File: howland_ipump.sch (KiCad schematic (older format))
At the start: 10 parts, among them U11 OPA991S

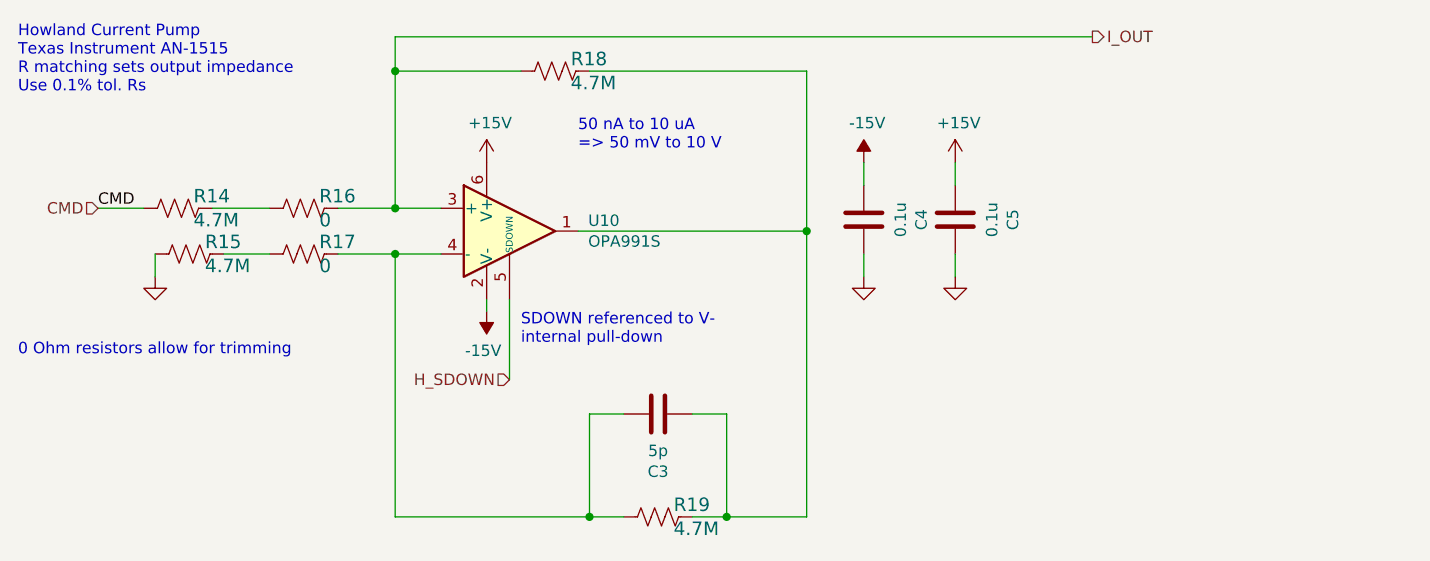
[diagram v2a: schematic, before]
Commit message: near complete top level schematic routing
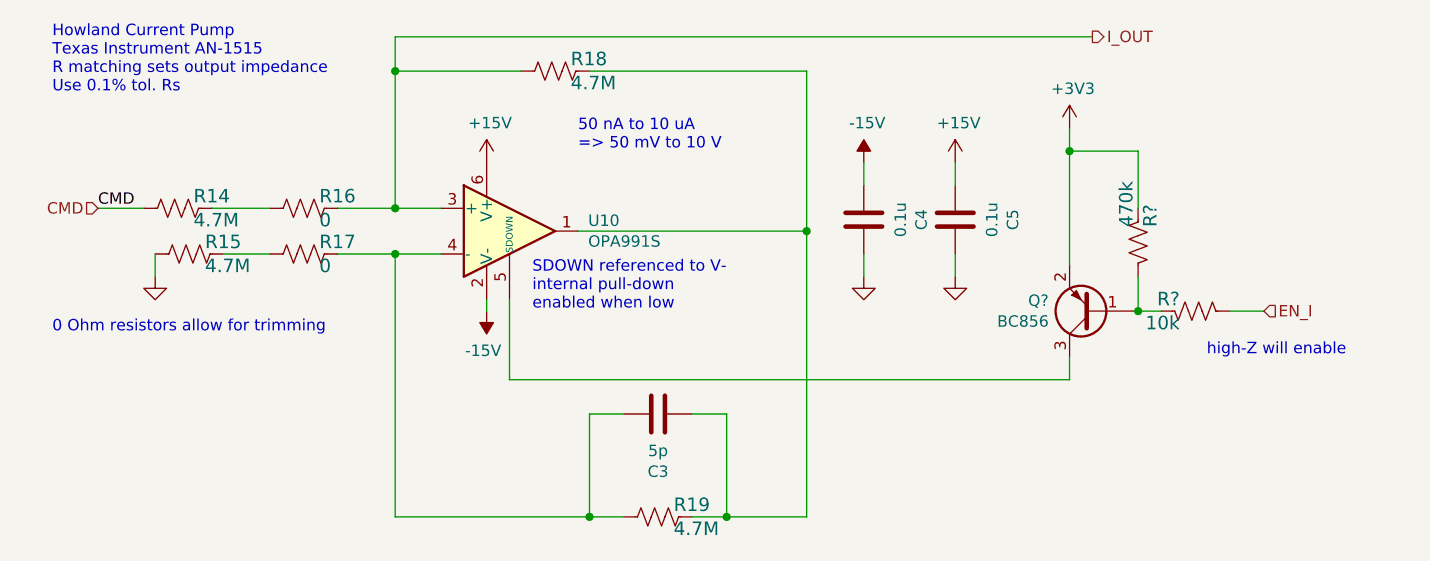
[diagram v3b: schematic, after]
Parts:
- added Q?: BC856, Package_TO_SOT_SMD:SOT-23, symbol Transistor_BJT:BC856
- added R?: 10k, Resistor_SMD:R_0603_1608Metric, symbol Device:R_US
- added R?: 470k, Resistor_SMD:R_0603_1608Metric, symbol Device:R_US
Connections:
- net H_SDOWN: no longer names the net of U11.5 (SDOWN)
- net H_SDOWN: now also Q?.3 (C)
- new net: Q?.1 (B), R?.1, R?.2
- new net +3V3: Q?.2 (E), R?.1
- new net EN_I: R?.2
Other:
- note added: "SDOWN referenced to V-\ninternal pull-down\nenabled when low\n"
- note added: "high-Z will enable"
- note removed: "SDOWN referenced to V-\ninternal pull-down\n"
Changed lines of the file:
@@
 $Descr A4 11693 8268
 encoding utf-8
-Sheet 4 18
+Sheet 3 18
 Title ""
 Date ""
@@
 AR Path="/6095BD4C/60BE01FC/60D781E3" Ref="#PWR0116"  Part="1"
 AR Path="/6095BD4C/60C5A41E/60D781E3" Ref="#PWR?"  Part="1"
+AR Path="/61B02572/60BE01FC/60D781E3" Ref="#PWR?"  Part="1"
 F 0 "#PWR0116" H 5100 4150 50  0001 C CNN
 F 1 "-15V" H 5115 4223 50  0000 C CNN
@@
 AR Path="/6095BD4C/60BE01FC/60D781E9" Ref="#PWR0157"  Part="1"
 AR Path="/6095BD4C/60C5A41E/60D781E9" Ref="#PWR?"  Part="1"
+AR Path="/61B02572/60BE01FC/60D781E9" Ref="#PWR?"  Part="1"
 F 0 "#PWR0157" H 5100 3250 50  0001 C CNN
 F 1 "+15V" H 5115 3573 50  0000 C CNN
@@
 AR Path="/6095BD4C/60BE01FC/60D781F4" Ref="C3"  Part="1"
 AR Path="/6095BD4C/60C5A41E/60D781F4" Ref="C?"  Part="1"
+AR Path="/61B02572/60BE01FC/60D781F4" Ref="C?"  Part="1"
 F 0 "C3" V 5598 4500 50  0000 C CNN
 F 1 "5p" V 5689 4500 50  0000 C CNN
@@
 AR Path="/6095BD4C/60BE01FC/60D78215" Ref="#PWR0158"  Part="1"
 AR Path="/6095BD4C/60C5A41E/60D78215" Ref="#PWR?"  Part="1"
+AR Path="/61B02572/60BE01FC/60D78215" Ref="#PWR?"  Part="1"
 F 0 "#PWR0158" H 3650 3650 50  0001 C CNN
 F 1 "GND" V 3655 3772 50  0001 R CNN
@@
 AR Path="/6095BD4C/60BE01FC/60D7821F" Ref="U10"  Part="1"
 AR Path="/6095BD4C/60C5A41E/60D7821F" Ref="U?"  Part="1"
+AR Path="/61B02572/60BE01FC/60D7821F" Ref="U?"  Part="1"
 F 0 "U10" H 5544 3746 50  0000 L CNN
 F 1 "OPA991S" H 5544 3655 50  0000 L CNN
@@
 Wire Wire Line
 	5550 3000 6500 3000
-Text Notes 5250 4200 0    50   ~ 0
-SDOWN referenced to V-\ninternal pull-down\n
-Wire Wire Line
-	5200 4000 5200 4350
+Text Notes 5300 4050 0    50   ~ 0
+SDOWN referenced to V-\ninternal pull-down\nenabled when low\n
 Text Notes 5500 3350 0    50   ~ 0
 50 nA to 10 uA\n=> 50 mV to 10 V
@@
 AR Path="/6095BD4C/60BE01FC/60D78240" Ref="R19"  Part="1"
 AR Path="/6095BD4C/60C5A41E/60D78240" Ref="R?"  Part="1"
+AR Path="/61B02572/60BE01FC/60D78240" Ref="R?"  Part="1"
 F 0 "R19" V 5797 5018 59  0000 L CNN
 F 1 "4.7M" V 5902 5018 59  0000 L CNN
@@
 	0    1    1    0
 $EndComp
-Text Notes 3050 3100 0    50   ~ 0
+Text Notes 3200 3100 0    50   ~ 0
 Howland Current Pump\nTexas Instrument AN-1515\nR matching sets output impedance\nUse 0.1% tol. Rs
 $Comp
@@
 AR Path="/6095BD4C/60BE01FC/60D7824A" Ref="C4"  Part="1"
 AR Path="/6095BD4C/60C5A41E/60D7824A" Ref="C?"  Part="1"
+AR Path="/61B02572/60BE01FC/60D7824A" Ref="C?"  Part="1"
 F 0 "C4" V 6498 3650 50  0000 C CNN
 F 1 "0.1u" V 6589 3650 50  0000 C CNN
@@
 AR Path="/6095BD4C/60BE01FC/60D78250" Ref="#PWR0163"  Part="1"
 AR Path="/6095BD4C/60C5A41E/60D78250" Ref="#PWR?"  Part="1"
+AR Path="/61B02572/60BE01FC/60D78250" Ref="#PWR?"  Part="1"
 F 0 "#PWR0163" H 6750 3650 50  0001 C CNN
 F 1 "GND" V 6755 3772 50  0001 R CNN
@@
 AR Path="/6095BD4C/60BE01FC/60D78256" Ref="#PWR0164"  Part="1"
 AR Path="/6095BD4C/60C5A41E/60D78256" Ref="#PWR?"  Part="1"
+AR Path="/61B02572/60BE01FC/60D78256" Ref="#PWR?"  Part="1"
 F 0 "#PWR0164" H 7150 3250 50  0001 C CNN
 F 1 "+15V" H 7165 3573 50  0000 C CNN
@@
 AR Path="/6095BD4C/60BE01FC/60D7825C" Ref="#PWR0165"  Part="1"
 AR Path="/6095BD4C/60C5A41E/60D7825C" Ref="#PWR?"  Part="1"
+AR Path="/61B02572/60BE01FC/60D7825C" Ref="#PWR?"  Part="1"
 F 0 "#PWR0165" H 7150 3650 50  0001 C CNN
 F 1 "GND" V 7155 3772 50  0001 R CNN
@@
 AR Path="/6095BD4C/60BE01FC/60D78264" Ref="C5"  Part="1"
 AR Path="/6095BD4C/60C5A41E/60D78264" Ref="C?"  Part="1"
+AR Path="/61B02572/60BE01FC/60D78264" Ref="C?"  Part="1"
 F 0 "C5" V 6898 3650 50  0000 C CNN
 F 1 "0.1u" V 6989 3650 50  0000 C CNN
@@
 AR Path="/6095BD4C/60BE01FC/60D7826A" Ref="#PWR0166"  Part="1"
 AR Path="/6095BD4C/60C5A41E/60D7826A" Ref="#PWR?"  Part="1"
+AR Path="/61B02572/60BE01FC/60D7826A" Ref="#PWR?"  Part="1"
 F 0 "#PWR0166" H 6750 3500 50  0001 C CNN
 F 1 "-15V" H 6765 3573 50  0000 C CNN
@@
 Text HLabel 3400 3600 0    50   Input ~ 0
 CMD
-Text HLabel 5200 4350 0    50   Input ~ 0
-H_SDOWN
 Wire Wire Line
 	5550 4500 5700 4500
@@
 AR Path="/6095BD4C/60BE01FC/60D83006" Ref="R17"  Part="1"
 AR Path="/6095BD4C/60C5A41E/60D83006" Ref="R?"  Part="1"
+AR Path="/61B02572/60BE01FC/60D83006" Ref="R?"  Part="1"
 F 0 "R17" V 4247 3868 59  0000 L CNN
 F 1 "0" V 4352 3868 59  0000 L CNN
@@
 AR Path="/6095BD4C/60BE01FC/60D8879F" Ref="R16"  Part="1"
 AR Path="/6095BD4C/60C5A41E/60D8879F" Ref="R?"  Part="1"
+AR Path="/61B02572/60BE01FC/60D8879F" Ref="R?"  Part="1"
 F 0 "R16" V 4247 3668 59  0000 L CNN
 F 1 "0" V 4352 3668 59  0000 L CNN
@@
 	4450 3600 4700 3600
 Connection ~ 4700 3600
-Text Notes 3050 4250 0    50   ~ 0
+Text Notes 3200 4150 0    50   ~ 0
 0 Ohm resistors allow for trimming
 $Comp
@@
 AR Path="/6095BD4C/60BE01FC/60B385AE" Ref="R15"  Part="1"
 AR Path="/6095BD4C/60C5A41E/60B385AE" Ref="R?"  Part="1"
+AR Path="/61B02572/60BE01FC/60B385AE" Ref="R?"  Part="1"
 F 0 "R15" V 3747 3868 59  0000 L CNN
 F 1 "4.7M" V 3852 3868 59  0000 L CNN
@@
 AR Path="/6095BD4C/60BE01FC/60B38EA4" Ref="R14"  Part="1"
 AR Path="/6095BD4C/60C5A41E/60B38EA4" Ref="R?"  Part="1"
+AR Path="/61B02572/60BE01FC/60B38EA4" Ref="R?"  Part="1"
 F 0 "R14" V 3697 3668 59  0000 L CNN
 F 1 "4.7M" V 3802 3668 59  0000 L CNN
@@
 AR Path="/6095BD4C/60BE01FC/60B3940D" Ref="R18"  Part="1"
 AR Path="/6095BD4C/60C5A41E/60B3940D" Ref="R?"  Part="1"
+AR Path="/61B02572/60BE01FC/60B3940D" Ref="R?"  Part="1"
 F 0 "R18" V 5347 3068 59  0000 L CNN
 F 1 "4.7M" V 5452 3068 59  0000 L CNN
@@
 	0    1    1    0
 $EndComp
+$Comp
+L Transistor_BJT:BC856 Q?
+U 1 1 60BEDC00
+P 7750 4050
+F 0 "Q?" H 7941 4004 50  0000 L CNN
+F 1 "BC856" H 7941 4095 50  0000 L CNN
+F 2 "Package_TO_SOT_SMD:SOT-23" H 7950 3975 50  0001 L CIN
+F 3 "https://www.onsemi.com/pub/Collateral/BC860-D.pdf" H 7750 4050 50  0001 L CNN
+	1    7750 4050
+	-1   0    0    1
+$EndComp
+$Comp
+L Device:R_US R?
+U 1 1 60BF0E09
+P 8200 4050
+AR Path="/6032F251/60BF0E09" Ref="R?"  Part="1"
+AR Path="/6032F251/60BDCE3E/60BF0E09" Ref="R?"  Part="1"
+AR Path="/6095BD4C/60BE01FC/60BF0E09" Ref="R?"  Part="1"
+AR Path="/6095BD4C/60C5A41E/60BF0E09" Ref="R?"  Part="1"
+AR Path="/61B02572/60BE01FC/60BF0E09" Ref="R?"  Part="1"
+F 0 "R?" V 8147 4118 59  0000 L CNN
+F 1 "10k" V 8252 4118 59  0000 L CNN
+F 2 "Resistor_SMD:R_0603_1608Metric" H 8200 4050 50  0001 C CNN
+F 3 "" H 8200 4050 50  0001 C CNN
+F 4 "RC0603FR-0710KL" H 8147 4218 50  0001 C CNN "Manf#"
+F 5 "0.1" H 8200 4050 50  0001 C CNN "Tolerance"
+	1    8200 4050
+	0    -1   1    0
+$EndComp
+$Comp
+L power:+3V3 #PWR?
+U 1 1 60BF2F91
+P 7650 3250
+F 0 "#PWR?" H 7650 3100 50  0001 C CNN
+F 1 "+3V3" H 7665 3423 50  0000 C CNN
+F 2 "" H 7650 3250 50  0001 C CNN
+F 3 "" H 7650 3250 50  0001 C CNN
+	1    7650 3250
+	1    0    0    -1
+$EndComp
+Wire Wire Line
+	7950 4050 8050 4050
+Wire Wire Line
+	8350 4050 8500 4050
+Wire Wire Line
+	5200 4000 5200 4350
+Wire Wire Line
+	5200 4350 7650 4350
+Wire Wire Line
+	7650 4350 7650 4250
+Text HLabel 8500 4050 2    50   Input ~ 0
+EN_I
+Wire Wire Line
+	7650 3250 7650 3350
+$Comp
+L Device:R_US R?
+U 1 1 60C16A39
+P 7950 3750
+AR Path="/6032F251/60C16A39" Ref="R?"  Part="1"
+AR Path="/6032F251/60BDCE3E/60C16A39" Ref="R?"  Part="1"
+AR Path="/6095BD4C/60BE01FC/60C16A39" Ref="R?"  Part="1"
+AR Path="/6095BD4C/60C5A41E/60C16A39" Ref="R?"  Part="1"
+AR Path="/61B02572/60BE01FC/60C16A39" Ref="R?"  Part="1"
+F 0 "R?" V 7897 3818 59  0000 L CNN
+F 1 "470k" V 8002 3818 59  0000 L CNN
+F 2 "Resistor_SMD:R_0603_1608Metric" H 7950 3750 50  0001 C CNN
+F 3 "" H 7950 3750 50  0001 C CNN
+F 4 "RC0603FR-0710KL" H 7897 3918 50  0001 C CNN "Manf#"
+F 5 "0.1" H 7950 3750 50  0001 C CNN "Tolerance"
+	1    7950 3750
+	-1   0    0    -1
+$EndComp
+Wire Wire Line
+	7950 4050 7950 3900
+Connection ~ 7950 4050
+Wire Wire Line
+	7650 3350 7950 3350
+Wire Wire Line
+	7950 3350 7950 3600
+Connection ~ 7650 3350
+Wire Wire Line
+	7650 3350 7650 3850
+Text Notes 8250 4250 0    50   ~ 0
+high-Z will enable
 $EndSCHEMATC

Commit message: corrected most ERC errors
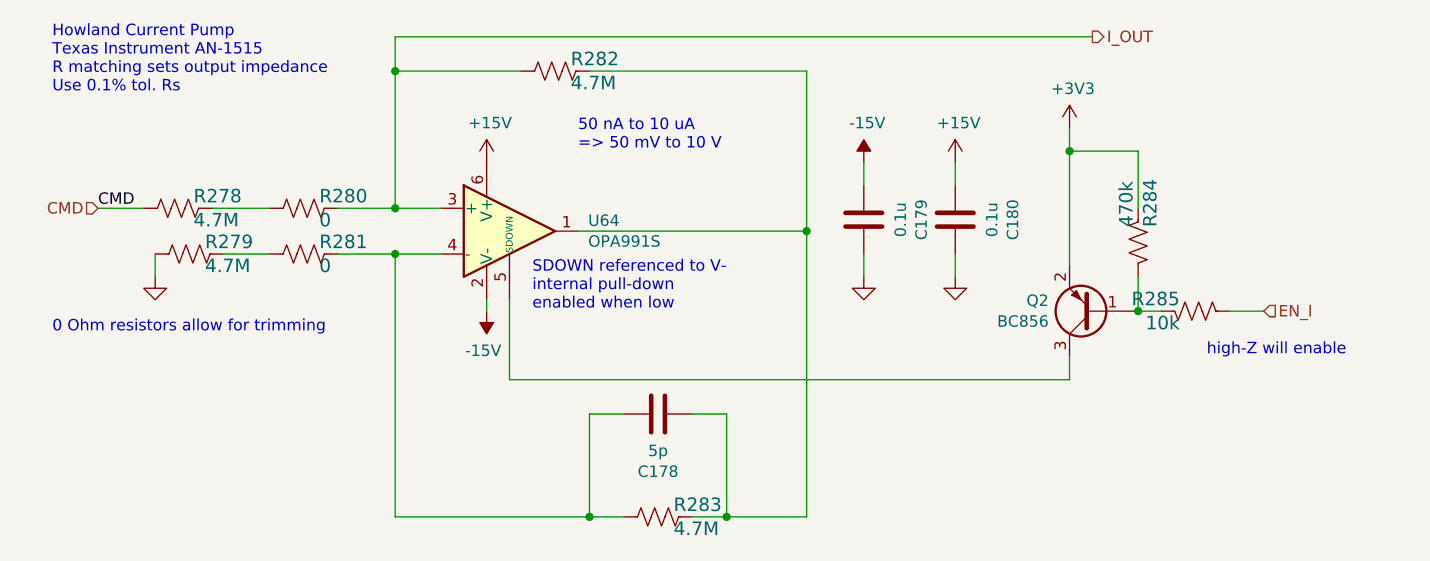
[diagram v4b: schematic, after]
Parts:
- gave numbers to parts that had none: 3
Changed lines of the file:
@@
 AR Path="/6095BD4C/60BE01FC/60D781E3" Ref="#PWR0116"  Part="1"
 AR Path="/6095BD4C/60C5A41E/60D781E3" Ref="#PWR?"  Part="1"
-AR Path="/61B02572/60BE01FC/60D781E3" Ref="#PWR?"  Part="1"
-F 0 "#PWR0116" H 5100 4150 50  0001 C CNN
+AR Path="/61B02572/60BE01FC/60D781E3" Ref="#PWR0331"  Part="1"
+F 0 "#PWR0331" H 5100 4150 50  0001 C CNN
 F 1 "-15V" H 5115 4223 50  0000 C CNN
 F 2 "" H 5100 4050 50  0001 C CNN
@@
 AR Path="/6095BD4C/60BE01FC/60D781E9" Ref="#PWR0157"  Part="1"
 AR Path="/6095BD4C/60C5A41E/60D781E9" Ref="#PWR?"  Part="1"
-AR Path="/61B02572/60BE01FC/60D781E9" Ref="#PWR?"  Part="1"
-F 0 "#PWR0157" H 5100 3250 50  0001 C CNN
+AR Path="/61B02572/60BE01FC/60D781E9" Ref="#PWR0332"  Part="1"
+F 0 "#PWR0332" H 5100 3250 50  0001 C CNN
 F 1 "+15V" H 5115 3573 50  0000 C CNN
 F 2 "" H 5100 3400 50  0001 C CNN
@@
 AR Path="/6095BD4C/60BE01FC/60D781F4" Ref="C3"  Part="1"
 AR Path="/6095BD4C/60C5A41E/60D781F4" Ref="C?"  Part="1"
-AR Path="/61B02572/60BE01FC/60D781F4" Ref="C?"  Part="1"
-F 0 "C3" V 5598 4500 50  0000 C CNN
+AR Path="/61B02572/60BE01FC/60D781F4" Ref="C178"  Part="1"
+F 0 "C178" V 5598 4500 50  0000 C CNN
 F 1 "5p" V 5689 4500 50  0000 C CNN
 F 2 "Capacitor_SMD:C_0603_1608Metric" H 5888 4350 50  0001 C CNN
@@
 AR Path="/6095BD4C/60BE01FC/60D78215" Ref="#PWR0158"  Part="1"
 AR Path="/6095BD4C/60C5A41E/60D78215" Ref="#PWR?"  Part="1"
-AR Path="/61B02572/60BE01FC/60D78215" Ref="#PWR?"  Part="1"
-F 0 "#PWR0158" H 3650 3650 50  0001 C CNN
+AR Path="/61B02572/60BE01FC/60D78215" Ref="#PWR0333"  Part="1"
+F 0 "#PWR0333" H 3650 3650 50  0001 C CNN
 F 1 "GND" V 3655 3772 50  0001 R CNN
 F 2 "" H 3650 3900 50  0001 C CNN
@@
 AR Path="/6095BD4C/60BE01FC/60D7821F" Ref="U10"  Part="1"
 AR Path="/6095BD4C/60C5A41E/60D7821F" Ref="U?"  Part="1"
-AR Path="/61B02572/60BE01FC/60D7821F" Ref="U?"  Part="1"
-F 0 "U10" H 5544 3746 50  0000 L CNN
+AR Path="/61B02572/60BE01FC/60D7821F" Ref="U64"  Part="1"
+F 0 "U64" H 5544 3746 50  0000 L CNN
 F 1 "OPA991S" H 5544 3655 50  0000 L CNN
 F 2 "Package_TO_SOT_SMD:SOT-23-6" H 5350 3450 50  0001 L CNN
@@
 AR Path="/6095BD4C/60BE01FC/60D78240" Ref="R19"  Part="1"
 AR Path="/6095BD4C/60C5A41E/60D78240" Ref="R?"  Part="1"
-AR Path="/61B02572/60BE01FC/60D78240" Ref="R?"  Part="1"
-F 0 "R19" V 5797 5018 59  0000 L CNN
+AR Path="/61B02572/60BE01FC/60D78240" Ref="R283"  Part="1"
+F 0 "R283" V 5797 5018 59  0000 L CNN
 F 1 "4.7M" V 5902 5018 59  0000 L CNN
 F 2 "Resistor_SMD:R_1206_3216Metric" H 5850 4950 50  0001 C CNN
@@
 AR Path="/6095BD4C/60BE01FC/60D7824A" Ref="C4"  Part="1"
 AR Path="/6095BD4C/60C5A41E/60D7824A" Ref="C?"  Part="1"
-AR Path="/61B02572/60BE01FC/60D7824A" Ref="C?"  Part="1"
-F 0 "C4" V 6498 3650 50  0000 C CNN
+AR Path="/61B02572/60BE01FC/60D7824A" Ref="C179"  Part="1"
+F 0 "C179" V 6498 3650 50  0000 C CNN
 F 1 "0.1u" V 6589 3650 50  0000 C CNN
 F 2 "Capacitor_SMD:C_0603_1608Metric" H 6788 3500 50  0001 C CNN
@@
 AR Path="/6095BD4C/60BE01FC/60D78250" Ref="#PWR0163"  Part="1"
 AR Path="/6095BD4C/60C5A41E/60D78250" Ref="#PWR?"  Part="1"
-AR Path="/61B02572/60BE01FC/60D78250" Ref="#PWR?"  Part="1"
-F 0 "#PWR0163" H 6750 3650 50  0001 C CNN
+AR Path="/61B02572/60BE01FC/60D78250" Ref="#PWR0334"  Part="1"
+F 0 "#PWR0334" H 6750 3650 50  0001 C CNN
 F 1 "GND" V 6755 3772 50  0001 R CNN
 F 2 "" H 6750 3900 50  0001 C CNN
@@
 AR Path="/6095BD4C/60BE01FC/60D78256" Ref="#PWR0164"  Part="1"
 AR Path="/6095BD4C/60C5A41E/60D78256" Ref="#PWR?"  Part="1"
-AR Path="/61B02572/60BE01FC/60D78256" Ref="#PWR?"  Part="1"
-F 0 "#PWR0164" H 7150 3250 50  0001 C CNN
+AR Path="/61B02572/60BE01FC/60D78256" Ref="#PWR0335"  Part="1"
+F 0 "#PWR0335" H 7150 3250 50  0001 C CNN
 F 1 "+15V" H 7165 3573 50  0000 C CNN
 F 2 "" H 7150 3400 50  0001 C CNN
@@
 AR Path="/6095BD4C/60BE01FC/60D7825C" Ref="#PWR0165"  Part="1"
 AR Path="/6095BD4C/60C5A41E/60D7825C" Ref="#PWR?"  Part="1"
-AR Path="/61B02572/60BE01FC/60D7825C" Ref="#PWR?"  Part="1"
-F 0 "#PWR0165" H 7150 3650 50  0001 C CNN
+AR Path="/61B02572/60BE01FC/60D7825C" Ref="#PWR0336"  Part="1"
+F 0 "#PWR0336" H 7150 3650 50  0001 C CNN
 F 1 "GND" V 7155 3772 50  0001 R CNN
 F 2 "" H 7150 3900 50  0001 C CNN
@@
 AR Path="/6095BD4C/60BE01FC/60D78264" Ref="C5"  Part="1"
 AR Path="/6095BD4C/60C5A41E/60D78264" Ref="C?"  Part="1"
-AR Path="/61B02572/60BE01FC/60D78264" Ref="C?"  Part="1"
-F 0 "C5" V 6898 3650 50  0000 C CNN
+AR Path="/61B02572/60BE01FC/60D78264" Ref="C180"  Part="1"
+F 0 "C180" V 6898 3650 50  0000 C CNN
 F 1 "0.1u" V 6989 3650 50  0000 C CNN
 F 2 "Capacitor_SMD:C_0603_1608Metric" H 7188 3500 50  0001 C CNN
@@
 AR Path="/6095BD4C/60BE01FC/60D7826A" Ref="#PWR0166"  Part="1"
 AR Path="/6095BD4C/60C5A41E/60D7826A" Ref="#PWR?"  Part="1"
-AR Path="/61B02572/60BE01FC/60D7826A" Ref="#PWR?"  Part="1"
-F 0 "#PWR0166" H 6750 3500 50  0001 C CNN
+AR Path="/61B02572/60BE01FC/60D7826A" Ref="#PWR0337"  Part="1"
+F 0 "#PWR0337" H 6750 3500 50  0001 C CNN
 F 1 "-15V" H 6765 3573 50  0000 C CNN
 F 2 "" H 6750 3400 50  0001 C CNN
@@
 AR Path="/6095BD4C/60BE01FC/60D83006" Ref="R17"  Part="1"
 AR Path="/6095BD4C/60C5A41E/60D83006" Ref="R?"  Part="1"
-AR Path="/61B02572/60BE01FC/60D83006" Ref="R?"  Part="1"
-F 0 "R17" V 4247 3868 59  0000 L CNN
+AR Path="/61B02572/60BE01FC/60D83006" Ref="R281"  Part="1"
+F 0 "R281" V 4247 3868 59  0000 L CNN
 F 1 "0" V 4352 3868 59  0000 L CNN
 F 2 "Resistor_SMD:R_0603_1608Metric" H 4300 3800 50  0001 C CNN
@@
 AR Path="/6095BD4C/60BE01FC/60D8879F" Ref="R16"  Part="1"
 AR Path="/6095BD4C/60C5A41E/60D8879F" Ref="R?"  Part="1"
-AR Path="/61B02572/60BE01FC/60D8879F" Ref="R?"  Part="1"
-F 0 "R16" V 4247 3668 59  0000 L CNN
+AR Path="/61B02572/60BE01FC/60D8879F" Ref="R280"  Part="1"
+F 0 "R280" V 4247 3668 59  0000 L CNN
 F 1 "0" V 4352 3668 59  0000 L CNN
 F 2 "Resistor_SMD:R_0603_1608Metric" H 4300 3600 50  0001 C CNN
@@
 AR Path="/6095BD4C/60BE01FC/60B385AE" Ref="R15"  Part="1"
 AR Path="/6095BD4C/60C5A41E/60B385AE" Ref="R?"  Part="1"
-AR Path="/61B02572/60BE01FC/60B385AE" Ref="R?"  Part="1"
-F 0 "R15" V 3747 3868 59  0000 L CNN
+AR Path="/61B02572/60BE01FC/60B385AE" Ref="R279"  Part="1"
+F 0 "R279" V 3747 3868 59  0000 L CNN
 F 1 "4.7M" V 3852 3868 59  0000 L CNN
 F 2 "Resistor_SMD:R_1206_3216Metric" H 3800 3800 50  0001 C CNN
@@
 AR Path="/6095BD4C/60BE01FC/60B38EA4" Ref="R14"  Part="1"
 AR Path="/6095BD4C/60C5A41E/60B38EA4" Ref="R?"  Part="1"
-AR Path="/61B02572/60BE01FC/60B38EA4" Ref="R?"  Part="1"
-F 0 "R14" V 3697 3668 59  0000 L CNN
+AR Path="/61B02572/60BE01FC/60B38EA4" Ref="R278"  Part="1"
+F 0 "R278" V 3697 3668 59  0000 L CNN
 F 1 "4.7M" V 3802 3668 59  0000 L CNN
 F 2 "Resistor_SMD:R_1206_3216Metric" H 3750 3600 50  0001 C CNN
@@
 AR Path="/6095BD4C/60BE01FC/60B3940D" Ref="R18"  Part="1"
 AR Path="/6095BD4C/60C5A41E/60B3940D" Ref="R?"  Part="1"
-AR Path="/61B02572/60BE01FC/60B3940D" Ref="R?"  Part="1"
-F 0 "R18" V 5347 3068 59  0000 L CNN
+AR Path="/61B02572/60BE01FC/60B3940D" Ref="R282"  Part="1"
+F 0 "R282" V 5347 3068 59  0000 L CNN
 F 1 "4.7M" V 5452 3068 59  0000 L CNN
 F 2 "Resistor_SMD:R_1206_3216Metric" H 5400 3000 50  0001 C CNN
@@
 $EndComp
 $Comp
-L Transistor_BJT:BC856 Q?
+L Transistor_BJT:BC856 Q1
 U 1 1 60BEDC00
 P 7750 4050
-F 0 "Q?" H 7941 4004 50  0000 L CNN
+AR Path="/6095BD4C/60BE01FC/60BEDC00" Ref="Q1"  Part="1"
+AR Path="/61B02572/60BE01FC/60BEDC00" Ref="Q2"  Part="1"
+F 0 "Q2" H 7941 4004 50  0000 L CNN
 F 1 "BC856" H 7941 4095 50  0000 L CNN
 F 2 "Package_TO_SOT_SMD:SOT-23" H 7950 3975 50  0001 L CIN
@@
 AR Path="/6032F251/60BF0E09" Ref="R?"  Part="1"
 AR Path="/6032F251/60BDCE3E/60BF0E09" Ref="R?"  Part="1"
-AR Path="/6095BD4C/60BE01FC/60BF0E09" Ref="R?"  Part="1"
+AR Path="/6095BD4C/60BE01FC/60BF0E09" Ref="R27"  Part="1"
 AR Path="/6095BD4C/60C5A41E/60BF0E09" Ref="R?"  Part="1"
-AR Path="/61B02572/60BE01FC/60BF0E09" Ref="R?"  Part="1"
-F 0 "R?" V 8147 4118 59  0000 L CNN
+AR Path="/61B02572/60BE01FC/60BF0E09" Ref="R285"  Part="1"
+F 0 "R285" V 8147 4118 59  0000 L CNN
 F 1 "10k" V 8252 4118 59  0000 L CNN
 F 2 "Resistor_SMD:R_0603_1608Metric" H 8200 4050 50  0001 C CNN
@@
 $EndComp
 $Comp
-L power:+3V3 #PWR?
+L power:+3V3 #PWR0160
 U 1 1 60BF2F91
 P 7650 3250
-F 0 "#PWR?" H 7650 3100 50  0001 C CNN
+AR Path="/6095BD4C/60BE01FC/60BF2F91" Ref="#PWR0160"  Part="1"
+AR Path="/61B02572/60BE01FC/60BF2F91" Ref="#PWR0338"  Part="1"
+F 0 "#PWR0338" H 7650 3100 50  0001 C CNN
 F 1 "+3V3" H 7665 3423 50  0000 C CNN
 F 2 "" H 7650 3250 50  0001 C CNN
@@
 AR Path="/6032F251/60C16A39" Ref="R?"  Part="1"
 AR Path="/6032F251/60BDCE3E/60C16A39" Ref="R?"  Part="1"
-AR Path="/6095BD4C/60BE01FC/60C16A39" Ref="R?"  Part="1"
+AR Path="/6095BD4C/60BE01FC/60C16A39" Ref="R26"  Part="1"
 AR Path="/6095BD4C/60C5A41E/60C16A39" Ref="R?"  Part="1"
-AR Path="/61B02572/60BE01FC/60C16A39" Ref="R?"  Part="1"
-F 0 "R?" V 7897 3818 59  0000 L CNN
+AR Path="/61B02572/60BE01FC/60C16A39" Ref="R284"  Part="1"
+F 0 "R284" V 7897 3818 59  0000 L CNN
 F 1 "470k" V 8002 3818 59  0000 L CNN
 F 2 "Resistor_SMD:R_0603_1608Metric" H 7950 3750 50  0001 C CNN
